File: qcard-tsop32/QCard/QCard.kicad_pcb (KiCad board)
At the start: 2 copper layers, 55 x 45 mm, 5 parts, among them J1 Conn_02x18_Top_Bottom, U1 SST39SF040

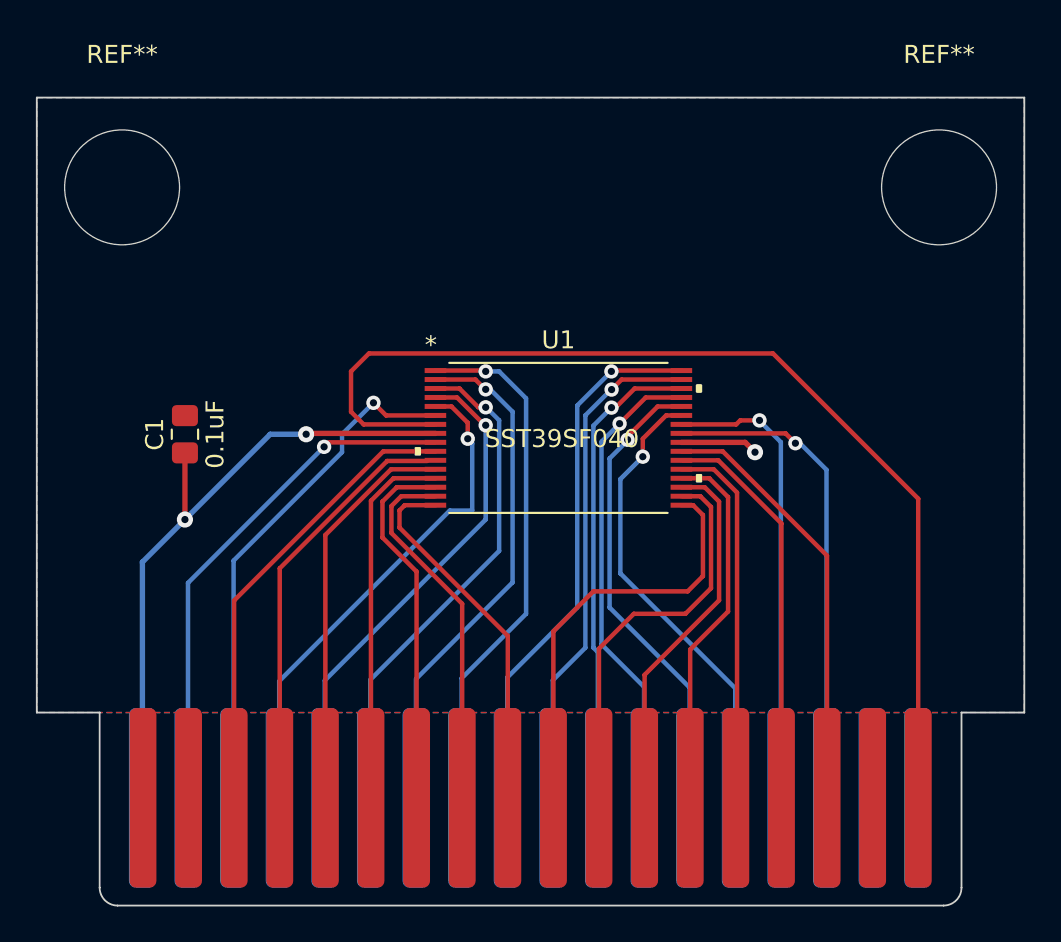
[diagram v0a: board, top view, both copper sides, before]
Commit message: Adds jumper for programming, fixes all DRC errors but loses mounting holes
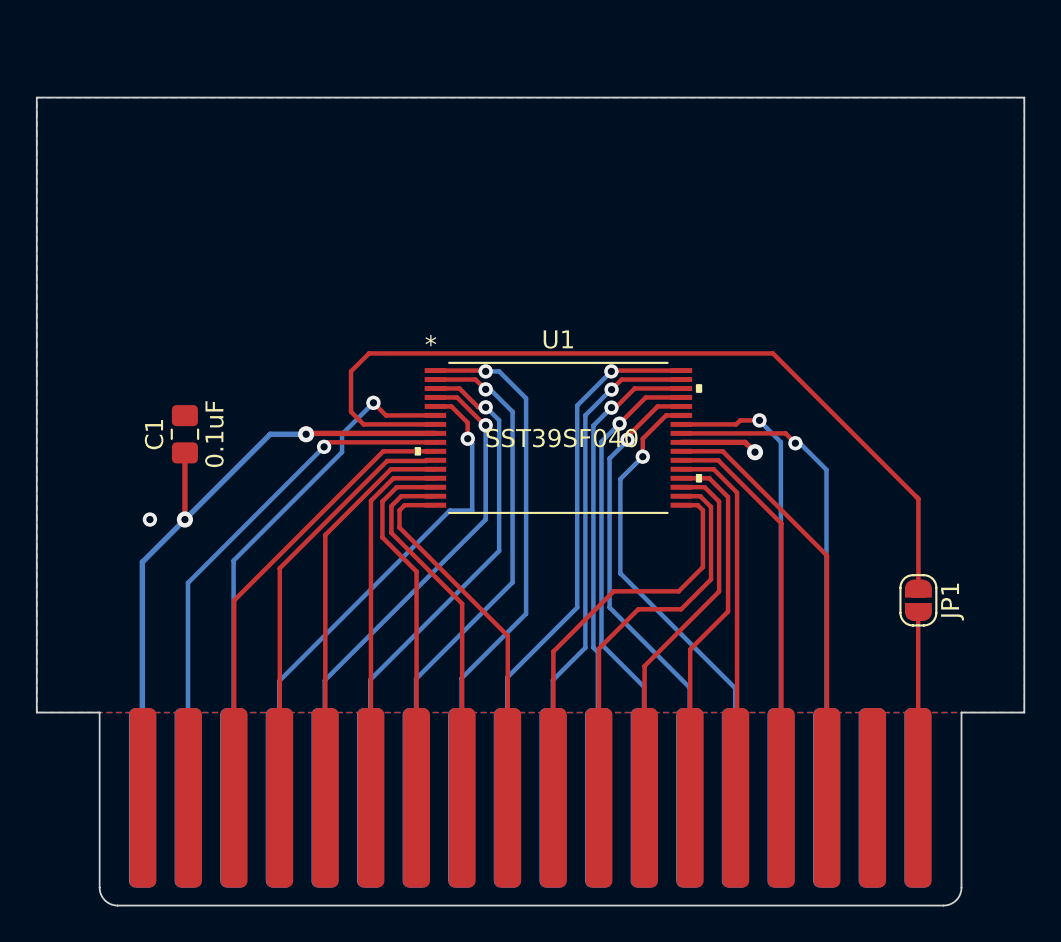
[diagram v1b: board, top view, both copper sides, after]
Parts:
- removed REF** (x2): MountingHole_6.4mm_M6, MountingHole:MountingHole_6.4mm_M6
- added JP1: SolderJumper_2_Open, Jumper:SolderJumper-2_P1.3mm_Open_RoundedPad1.0x1.5mm, F.Cu at (99.1, 78.0)
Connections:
- U1 pad 7: /PGM -> Net-(U1-Pad7)
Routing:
- net /PGM: track 59.3 -> 10.4 mm
- net Net-(U1-Pad7): track 0.00 -> 47.7 mm
- net /A3: track 23.7 -> 22.9 mm
- net /GND: vias 1 -> 2

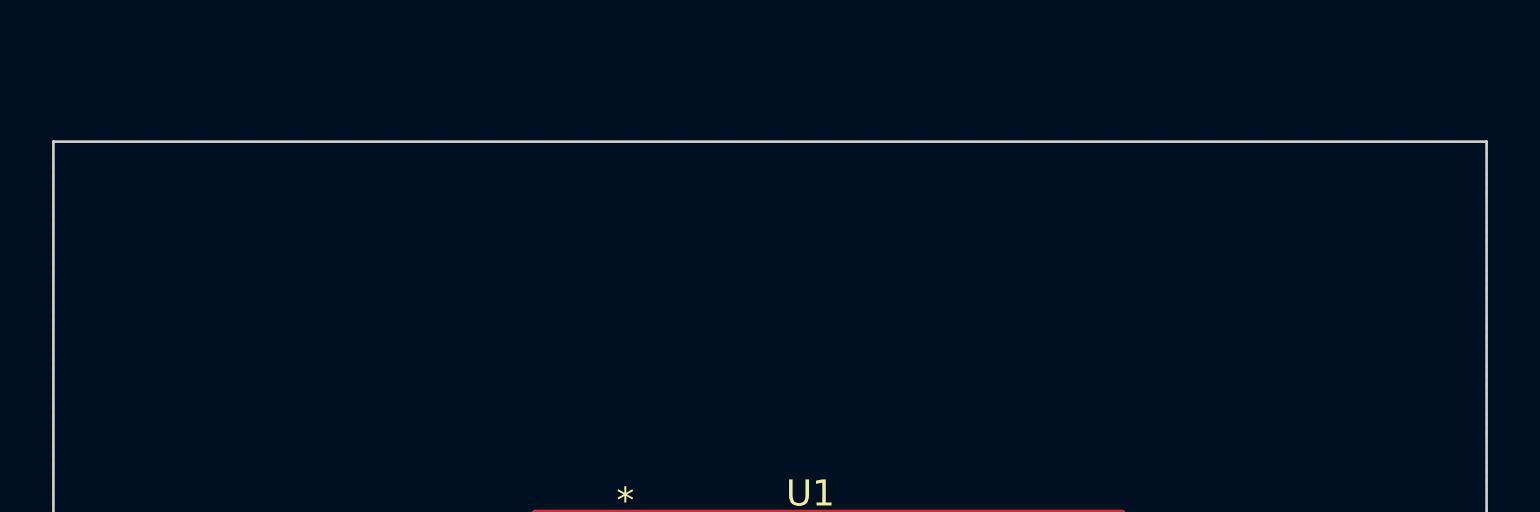
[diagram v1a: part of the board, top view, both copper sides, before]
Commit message: Restores mounting holes
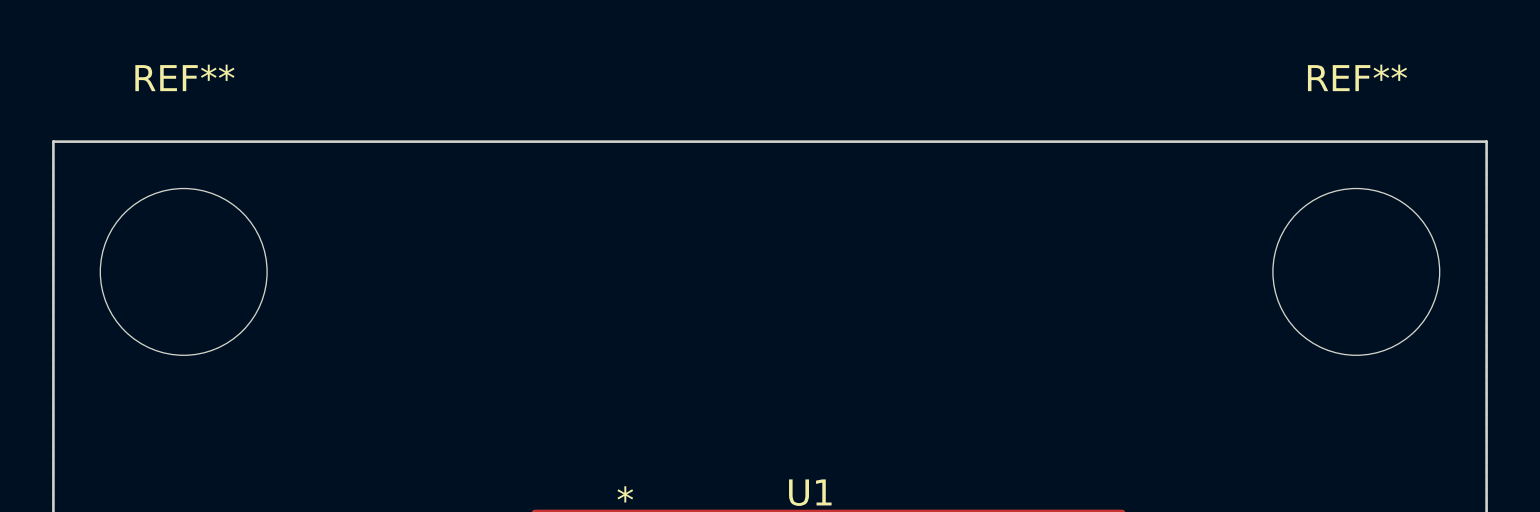
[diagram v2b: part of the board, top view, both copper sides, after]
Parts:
- added REF**: MountingHole_6.4mm_M6, MountingHole:MountingHole_6.4mm_M6, F.Cu at (55.0, 55.0)
- added REF**: MountingHole_6.4mm_M6, MountingHole:MountingHole_6.4mm_M6, F.Cu at (100.0, 55.0)
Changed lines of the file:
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@@
       ))
+  )
+  (footprint "MountingHole:MountingHole_6.4mm_M6" (layer "F.Cu")
+    (at 55 55)
+    (descr "Mounting Hole 6.4mm, no annular, M6")
+    (tags "mounting hole 6.4mm no annular m6")
+    (attr exclude_from_pos_files exclude_from_bom)
+    (fp_text reference "REF**" (at 0 -7.4) (layer "F.SilkS")
+      (effects (font (size 1 1) (thickness 0.15)))
+    )
+    (fp_text value "MountingHole_6.4mm_M6" (at 0 7.4) (layer "F.Fab")
+      (effects (font (size 1 1) (thickness 0.15)))
+    )
+    (fp_text user "${REFERENCE}" (at 0 0) (layer "F.Fab")
+      (effects (font (size 1 1) (thickness 0.15)))
+    )
+    (fp_circle (center 0 0) (end 6.4 0) (layer "Cmts.User") (width 0.15) (fill none))
+    (fp_circle (center 0 0) (end 6.65 0) (layer "F.CrtYd") (width 0.05) (fill none))
+    (pad "" np_thru_hole circle (at 0 0) (size 6.4 6.4) (drill 6.4) (layers *.Cu *.Mask))
   )
   (footprint "REB_Flash:SST39SF040-55-4C-WHE-T" locked (layer "F.Cu")
@@
     )
   )
+  (footprint "MountingHole:MountingHole_6.4mm_M6" (layer "F.Cu")
+    (at 100 55)
+    (descr "Mounting Hole 6.4mm, no annular, M6")
+    (tags "mounting hole 6.4mm no annular m6")
+    (attr exclude_from_pos_files exclude_from_bom)
+    (fp_text reference "REF**" (at 0 -7.4) (layer "F.SilkS")
+      (effects (font (size 1 1) (thickness 0.15)))
+    )
+    (fp_text value "MountingHole_6.4mm_M6" (at 0 7.4) (layer "F.Fab")
+      (effects (font (size 1 1) (thickness 0.15)))
+    )
+    (fp_text user "${REFERENCE}" (at 0 0) (layer "F.Fab")
+      (effects (font (size 1 1) (thickness 0.15)))
+    )
+    (fp_circle (center 0 0) (end 6.4 0) (layer "Cmts.User") (width 0.15) (fill none))
+    (fp_circle (center 0 0) (end 6.65 0) (layer "F.CrtYd") (width 0.05) (fill none))
+    (pad "" np_thru_hole circle (at 0 0) (size 6.4 6.4) (drill 6.4) (layers *.Cu *.Mask))
+  )
   (footprint "REB_Edge:REB_EdgeConnector_36pin" (layer "F.Cu")

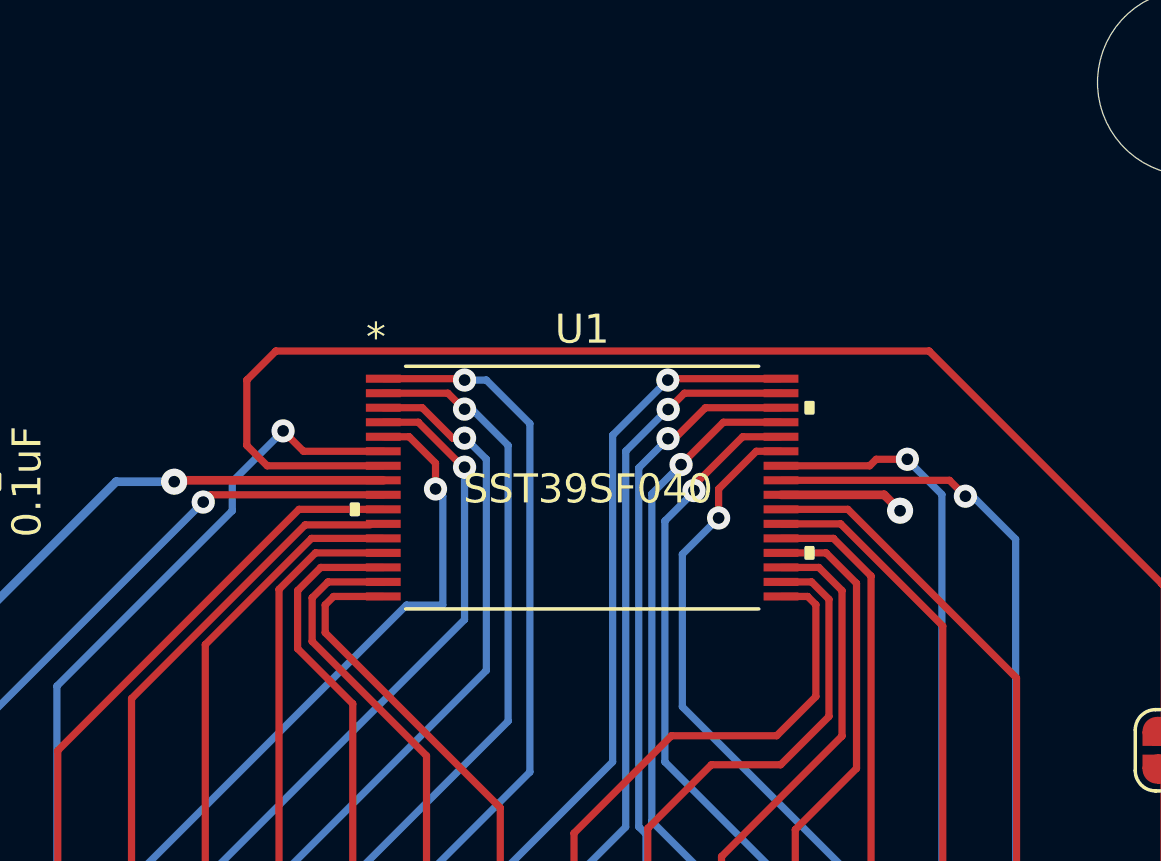
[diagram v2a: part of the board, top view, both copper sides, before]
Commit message: Adds label
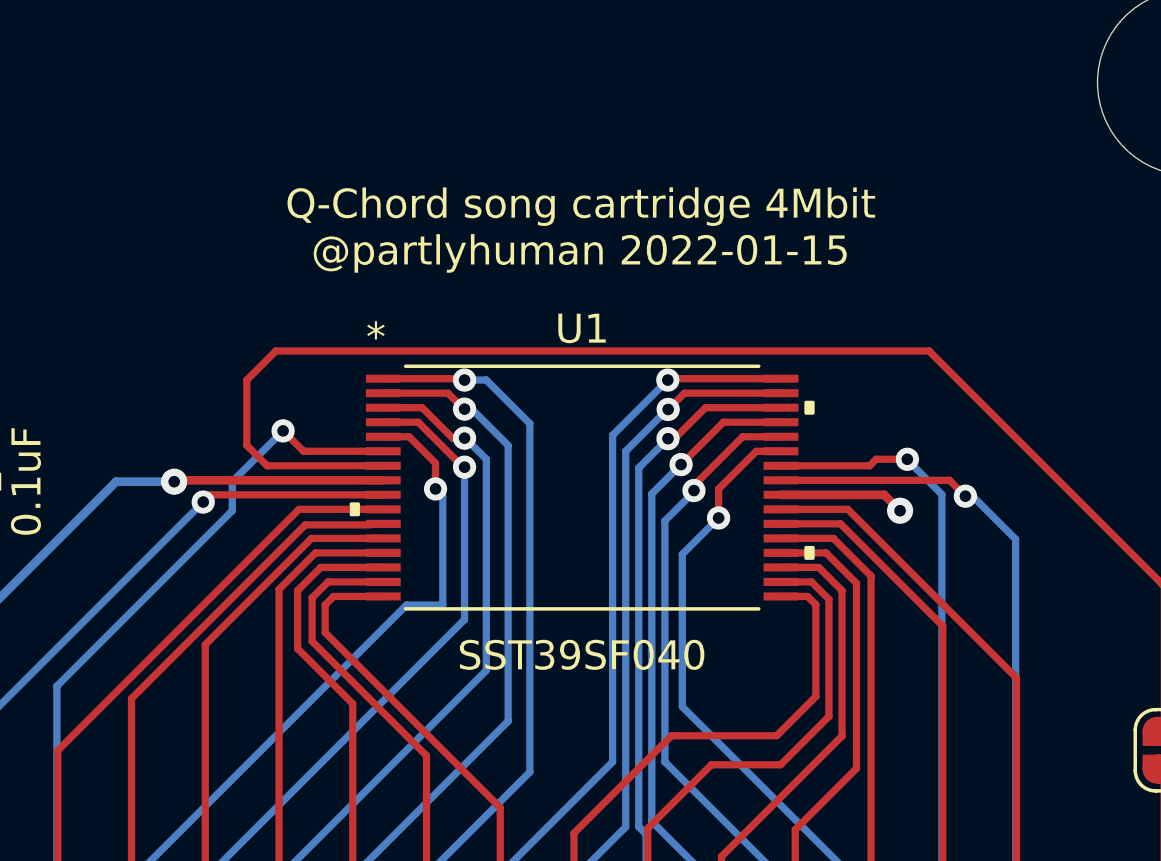
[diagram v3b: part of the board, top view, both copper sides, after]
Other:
- board text added: "Q-Chord song cartridge 4Mbit @partlyhuman 2022-01-15"
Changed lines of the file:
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@@
       (effects (font (size 1 1) (thickness 0.15)))
     )
-    (fp_text value "SST39SF040" (at 0.199775 0.0475) (layer "F.SilkS")
+    (fp_text value "SST39SF040" (at 0 5.7975) (layer "F.SilkS")
       (effects (font (size 1 1) (thickness 0.15)))
     )
@@
   (gr_line (start 53.5 84.25) (end 53.5 94) (layer "Edge.Cuts") (width 0.1))
   (gr_line (start 101.5 94) (end 101.5 84.25) (layer "Edge.Cuts") (width 0.1))
+  (gr_text "Q-Chord song cartridge 4Mbit\n@partlyhuman 2022-01-15" (at 79 60) (layer "F.SilkS")
+    (effects (font (size 1 1) (thickness 0.15)))
+  )
   (segment (start 65 68.75) (end 65.0475 68.7025) (width 0.3) (layer "F.Cu") (net 1))
   (segment (start 65.0475 68.7025) (end 72.201377 68.7025) (width 0.3) (layer "F.Cu") (net 1))

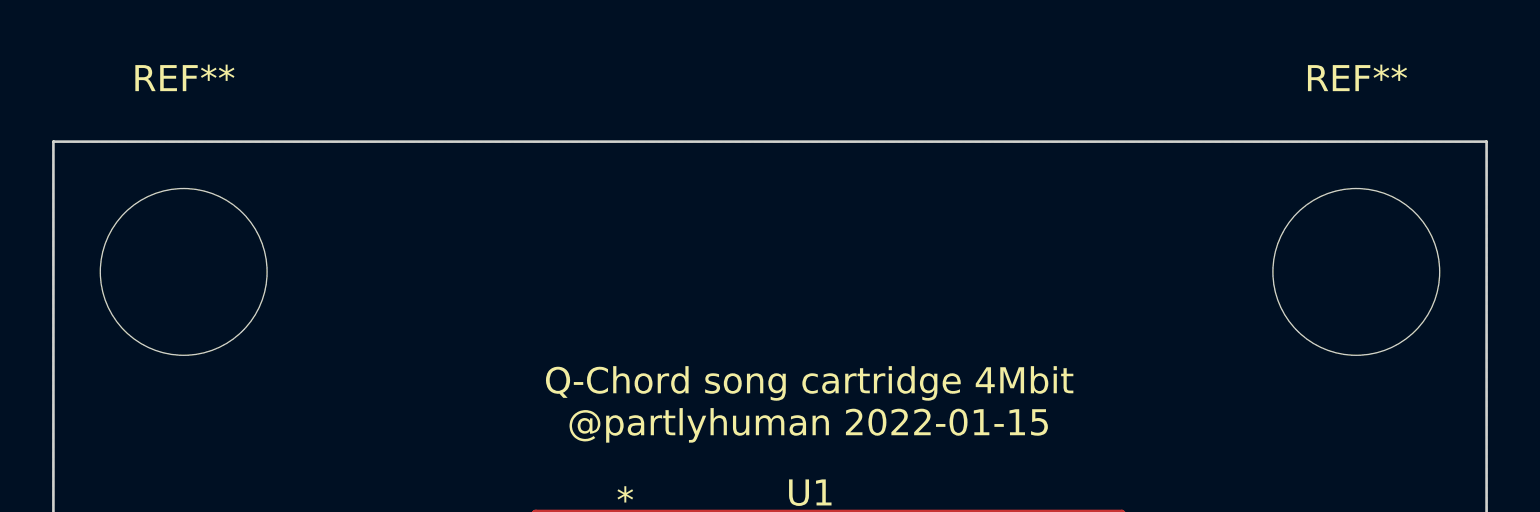
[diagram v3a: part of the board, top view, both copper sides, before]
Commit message: Nudge mounting holes
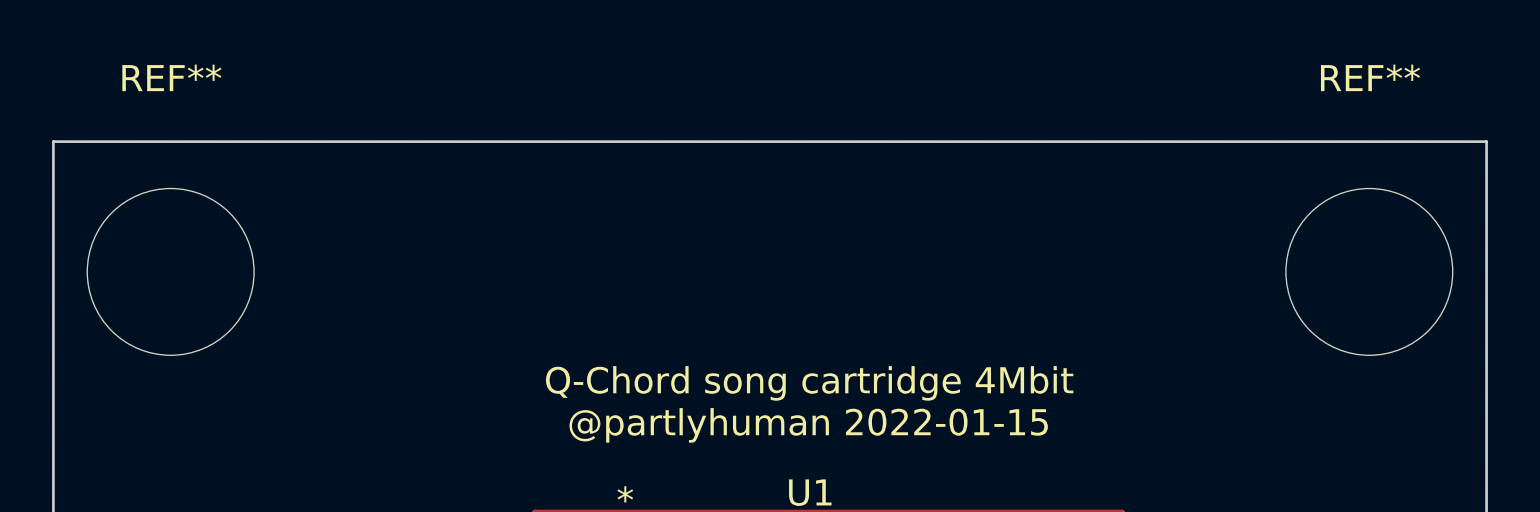
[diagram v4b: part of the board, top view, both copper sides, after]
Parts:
- moved REF** 0.50 mm to (54.5, 55.0)
- moved REF** 0.50 mm to (100.5, 55.0)
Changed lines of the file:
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@@
   )
   (footprint "MountingHole:MountingHole_6.4mm_M6" (layer "F.Cu")
-    (at 55 55)
+    (at 54.5 55)
     (descr "Mounting Hole 6.4mm, no annular, M6")
     (tags "mounting hole 6.4mm no annular m6")
@@
   )
   (footprint "MountingHole:MountingHole_6.4mm_M6" (layer "F.Cu")
-    (at 100 55)
+    (at 100.5 55)
     (descr "Mounting Hole 6.4mm, no annular, M6")
     (tags "mounting hole 6.4mm no annular m6")
